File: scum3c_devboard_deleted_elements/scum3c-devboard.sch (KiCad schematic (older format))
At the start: 11 parts, among them P1 Conn_01x03, U9AB1 MPU-9250

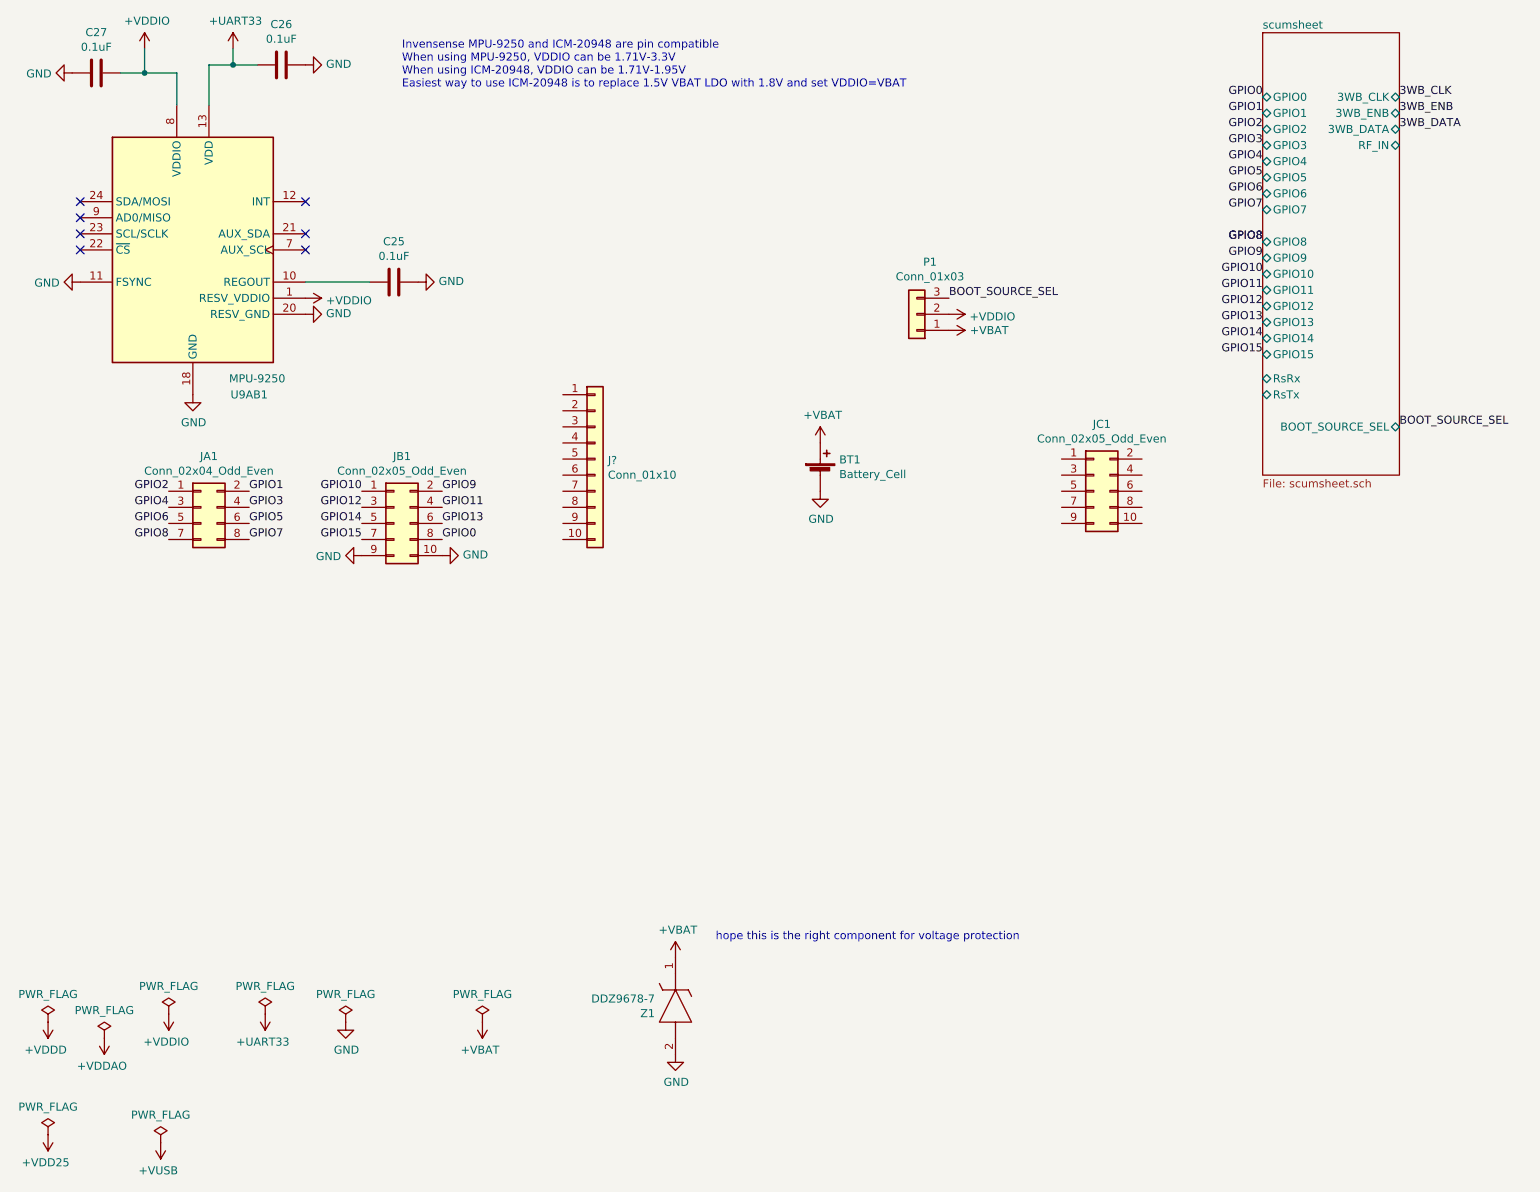
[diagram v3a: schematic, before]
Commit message: moved pins
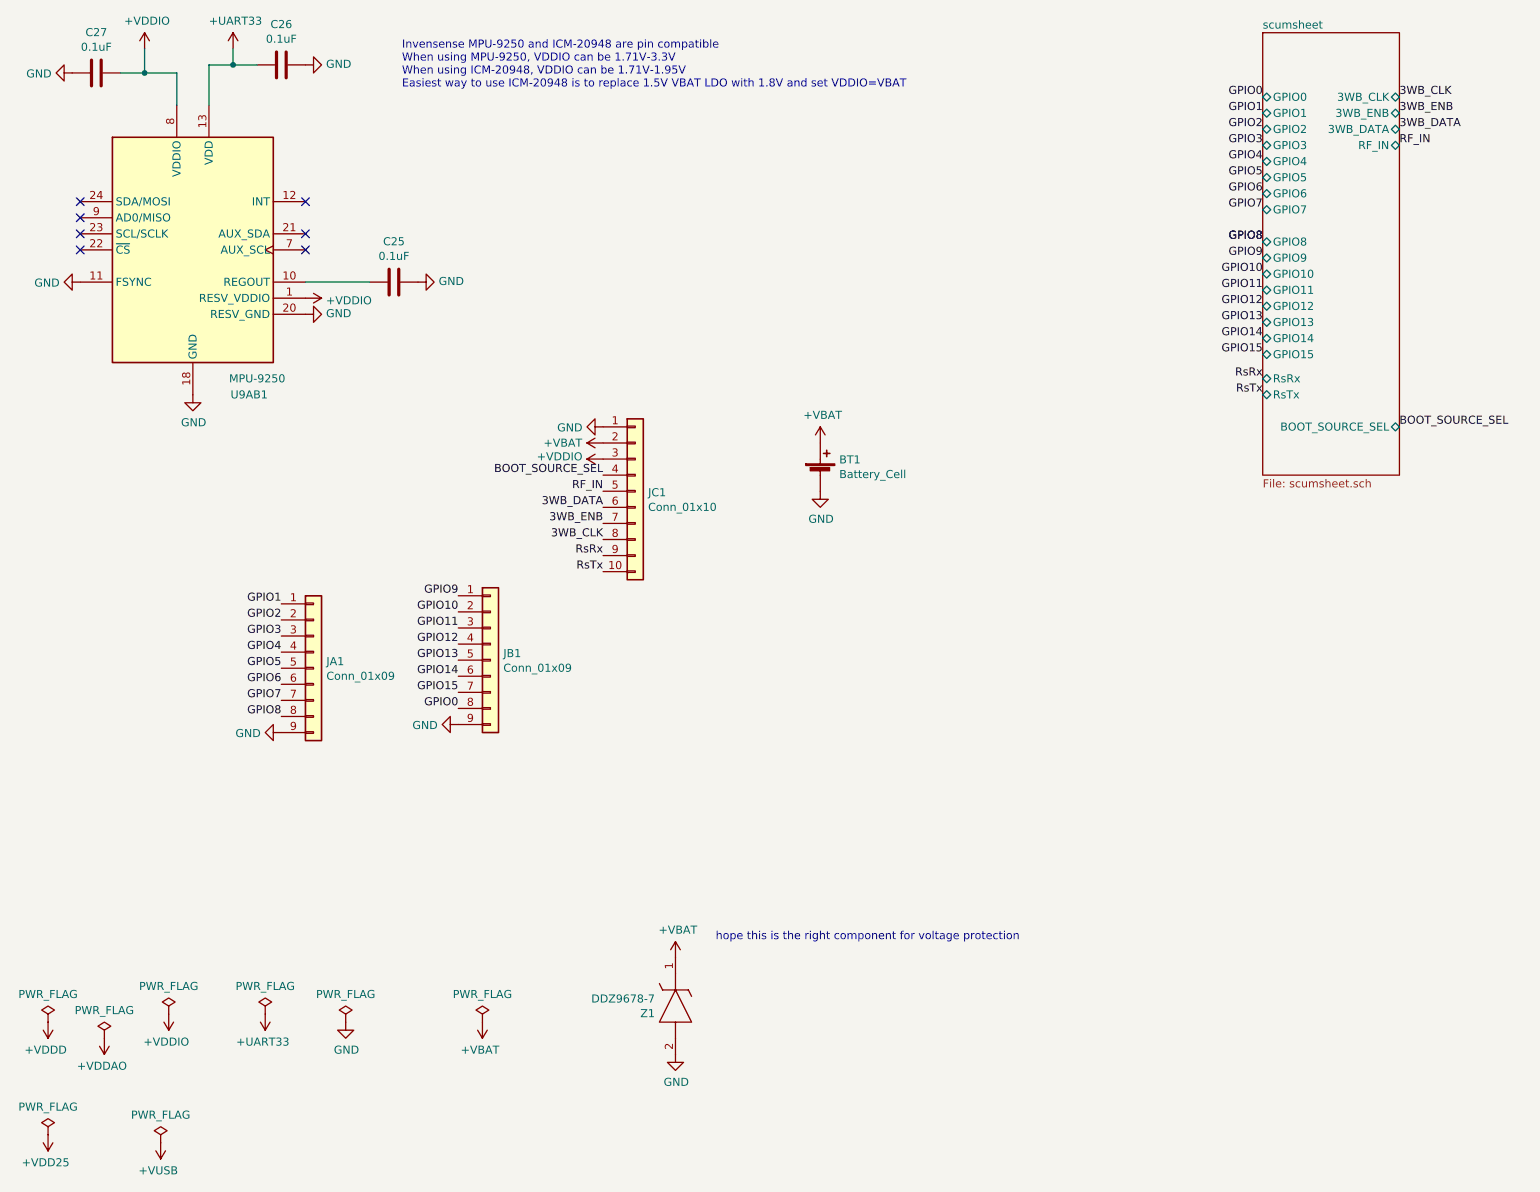
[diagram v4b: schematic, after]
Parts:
- removed JA1: Conn_02x04_Odd_Even, Connector_PinHeader_2.54mm:PinHeader_2x04_P2.54mm_Vertical, symbol Connector_Generic:Conn_02x04_Odd_Even
- removed JB1, JC1: Conn_02x05_Odd_Even, Connector_PinHeader_2.54mm:PinHeader_2x05_P2.54mm_Vertical, symbol Connector_Generic:Conn_02x05_Odd_Even
- removed P1: Conn_01x03, Connector_PinHeader_2.54mm:PinHeader_1x03_P2.54mm_Vertical, symbol Connector_Generic:Conn_01x03
- added JA1, JB1: Conn_01x09, Connector_PinHeader_2.54mm:PinHeader_1x09_P2.54mm_Vertical, symbol Connector_Generic:Conn_01x09
- JC1: renamed from J?; footprint (none) -> Connector_PinHeader_2.54mm:PinHeader_1x10_P2.54mm_Vertical
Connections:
- net +VBAT: now also JC1.2 (Pin_2)
- net +VDDIO: now also JC1.3 (Pin_3)
- net 3WB_CLK: now also JC1.8 (Pin_8)
- net 3WB_DATA: now also JC1.6 (Pin_6)
- net 3WB_ENB: now also JC1.7 (Pin_7)
- net BOOT_SOURCE_SEL: now also JC1.4 (Pin_4)
- net GND: now also JC1.1 (Pin_1), JA1.9 (Pin_9), JB1.9 (Pin_9)
- net GPIO0: now also JB1.8 (Pin_8)
- net GPIO1: now also JA1.1 (Pin_1)
- net GPIO10: now also JB1.2 (Pin_2)
- net GPIO11: now also JB1.3 (Pin_3)
- net GPIO12: now also JB1.4 (Pin_4)
- net GPIO13: now also JB1.5 (Pin_5)
- net GPIO14: now also JB1.6 (Pin_6)
- net GPIO15: now also JB1.7 (Pin_7)
- net GPIO2: now also JA1.2 (Pin_2)
- net GPIO3: now also JA1.3 (Pin_3)
- net GPIO4: now also JA1.4 (Pin_4)
- net GPIO5: now also JA1.5 (Pin_5)
- net GPIO6: now also JA1.6 (Pin_6)
- net GPIO7: now also JA1.7 (Pin_7)
- net GPIO8: now also JA1.8 (Pin_8)
- net GPIO9: now also JB1.1 (Pin_1)
- net RsTx: now reaches JC1.10 (Pin_10)
- net RF_IN: now reaches JC1.5 (Pin_5)
- net RsRx: now reaches JC1.9 (Pin_9)
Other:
- moved on the sheet: JC1
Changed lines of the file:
@@
 	1    0    0    -1
 $EndComp
-Text Label 2950 3650 2    50   ~ 0
+Text Label 3550 4400 2    50   ~ 0
 GPIO10
-Text Label 2950 3750 2    50   ~ 0
+Text Label 3550 4600 2    50   ~ 0
 GPIO12
-Text Label 2950 3850 2    50   ~ 0
+Text Label 3550 4800 2    50   ~ 0
 GPIO14
-Text Label 2950 3950 2    50   ~ 0
+Text Label 3550 4900 2    50   ~ 0
 GPIO15
 $Comp
 L power:GND #PWR0111
 U 1 1 5F3EC8B2
-P 2950 4050
-F 0 "#PWR0111" H 2950 3800 50  0001 C CNN
-F 1 "GND" V 2955 3922 50  0000 R CNN
-F 2 "" H 2950 4050 50  0001 C CNN
-F 3 "" H 2950 4050 50  0001 C CNN
-	1    2950 4050
+P 2450 5150
+F 0 "#PWR0111" H 2450 4900 50  0001 C CNN
+F 1 "GND" V 2455 5022 50  0000 R CNN
+F 2 "" H 2450 5150 50  0001 C CNN
+F 3 "" H 2450 5150 50  0001 C CNN
+	1    2450 5150
 	0    1    1    0
 $EndComp
-Text Label 3450 3650 0    50   ~ 0
+Text Label 3550 4300 2    50   ~ 0
 GPIO9
-Text Label 3450 3950 0    50   ~ 0
+Text Label 3550 5000 2    50   ~ 0
 GPIO0
-Text Label 3450 3850 0    50   ~ 0
+Text Label 3550 4700 2    50   ~ 0
 GPIO13
-Text Label 3450 3750 0    50   ~ 0
+Text Label 3550 4500 2    50   ~ 0
 GPIO11
 $Comp
 L power:GND #PWR0112
 U 1 1 5F3ED1BB
-P 3450 4050
-F 0 "#PWR0112" H 3450 3800 50  0001 C CNN
-F 1 "GND" V 3455 3922 50  0000 R CNN
-F 2 "" H 3450 4050 50  0001 C CNN
-F 3 "" H 3450 4050 50  0001 C CNN
-	1    3450 4050
-	0    -1   -1   0
+P 3550 5100
+F 0 "#PWR0112" H 3550 4850 50  0001 C CNN
+F 1 "GND" V 3555 4972 50  0000 R CNN
+F 2 "" H 3550 5100 50  0001 C CNN
+F 3 "" H 3550 5100 50  0001 C CNN
+	1    3550 5100
+	0    1    1    0
 $EndComp
 $Comp
@@
 	1    0    0    -1
 $EndComp
-$Comp
-L Connector_Generic:Conn_02x04_Odd_Even JA1
-U 1 1 5F4FC0F5
-P 1950 3750
-F 0 "JA1" H 2000 4067 50  0000 C CNN
-F 1 "Conn_02x04_Odd_Even" H 2000 3976 50  0000 C CNN
-F 2 "Connector_PinHeader_2.54mm:PinHeader_2x04_P2.54mm_Vertical" H 1950 3750 50  0001 C CNN
-F 3 "~" H 1950 3750 50  0001 C CNN
-	1    1950 3750
-	1    0    0    -1
-$EndComp
-$Comp
-L Connector_Generic:Conn_02x05_Odd_Even JB1
-U 1 1 5F4FD4BB
-P 3150 3850
-F 0 "JB1" H 3200 4267 50  0000 C CNN
-F 1 "Conn_02x05_Odd_Even" H 3200 4176 50  0000 C CNN
-F 2 "Connector_PinHeader_2.54mm:PinHeader_2x05_P2.54mm_Vertical" H 3150 3850 50  0001 C CNN
-F 3 "~" H 3150 3850 50  0001 C CNN
-	1    3150 3850
-	1    0    0    -1
-$EndComp
 Text Label 8550 2600 2    50   ~ 0
 GPIO13
@@
 L draft1library:+VBAT #PWR?
 U 1 1 5F7B958D
-P 6600 2650
+P 4450 3350
 AR Path="/5F3B1D81/5F7B958D" Ref="#PWR?"  Part="1"
 AR Path="/5F41418C/5F7B958D" Ref="#PWR?"  Part="1"
 AR Path="/5F414989/5F7B958D" Ref="#PWR?"  Part="1"
 AR Path="/5F7B958D" Ref="#PWR0109"  Part="1"
-F 0 "#PWR0109" H 6600 2500 50  0001 C CNN
-F 1 "+VBAT" V 6600 2900 50  0000 C CNN
-F 2 "" H 6600 2650 50  0001 C CNN
-F 3 "" H 6600 2650 50  0001 C CNN
-	1    6600 2650
-	0    1    1    0
-$EndComp
-Text Label 6600 2450 0    50   ~ 0
+F 0 "#PWR0109" H 4450 3200 50  0001 C CNN
+F 1 "+VBAT" V 4450 3600 50  0000 C CNN
+F 2 "" H 4450 3350 50  0001 C CNN
+F 3 "" H 4450 3350 50  0001 C CNN
+	1    4450 3350
+	0    -1   -1   0
+$EndComp
+Text Label 4450 3550 2    50   ~ 0
 BOOT_SOURCE_SEL
-$Comp
-L Connector_Generic:Conn_01x03 P?
-U 1 1 5F7B9594
-P 6400 2550
-AR Path="/5F3B1D81/5F7B9594" Ref="P?"  Part="1"
-AR Path="/5F7B9594" Ref="P1"  Part="1"
-F 0 "P1" H 6318 2225 50  0000 C CNN
-F 1 "Conn_01x03" H 6318 2316 50  0000 C CNN
-F 2 "Connector_PinHeader_2.54mm:PinHeader_1x03_P2.54mm_Vertical" H 6400 2550 50  0001 C CNN
-F 3 "~" H 6400 2550 50  0001 C CNN
-	1    6400 2550
-	-1   0    0    1
-$EndComp
 $Comp
 L draft1library:+VDDIO #PWR?
 U 1 1 5F7B959A
-P 6600 2550
+P 4450 3450
 AR Path="/5F3B1D81/5F7B959A" Ref="#PWR?"  Part="1"
 AR Path="/5F7B959A" Ref="#PWR0110"  Part="1"
-F 0 "#PWR0110" H 6600 2400 50  0001 C CNN
-F 1 "+VDDIO" V 6615 2678 50  0000 L CNN
-F 2 "" H 6600 2550 50  0001 C CNN
-F 3 "" H 6600 2550 50  0001 C CNN
-	1    6600 2550
-	0    1    1    0
+F 0 "#PWR0110" H 4450 3300 50  0001 C CNN
+F 1 "+VDDIO" V 4465 3578 50  0000 L CNN
+F 2 "" H 4450 3450 50  0001 C CNN
+F 3 "" H 4450 3450 50  0001 C CNN
+	1    4450 3450
+	0    -1   -1   0
 $EndComp
 Text Label 9400 3250 0    50   ~ 0
 BOOT_SOURCE_SEL
 $Comp
-L Connector_Generic:Conn_02x05_Odd_Even JC1
-U 1 1 5F7BA02A
-P 7500 3650
-F 0 "JC1" H 7550 4067 50  0000 C CNN
-F 1 "Conn_02x05_Odd_Even" H 7550 3976 50  0000 C CNN
-F 2 "Connector_PinHeader_2.54mm:PinHeader_2x05_P2.54mm_Vertical" H 7500 3650 50  0001 C CNN
-F 3 "~" H 7500 3650 50  0001 C CNN
-	1    7500 3650
-	1    0    0    -1
-$EndComp
-$Comp
-L Connector_Generic:Conn_01x10 J?
+L Connector_Generic:Conn_01x10 JC1
 U 1 1 5F7BC634
-P 4400 3450
-F 0 "J?" H 4480 3442 50  0000 L CNN
-F 1 "Conn_01x10" H 4480 3351 50  0000 L CNN
-F 2 "" H 4400 3450 50  0001 C CNN
-F 3 "~" H 4400 3450 50  0001 C CNN
-	1    4400 3450
-	1    0    0    -1
-$EndComp
-Text Label 2250 3750 0    50   ~ 0
+P 4650 3650
+F 0 "JC1" H 4730 3642 50  0000 L CNN
+F 1 "Conn_01x10" H 4730 3551 50  0000 L CNN
+F 2 "Connector_PinHeader_2.54mm:PinHeader_1x10_P2.54mm_Vertical" H 4650 3650 50  0001 C CNN
+F 3 "~" H 4650 3650 50  0001 C CNN
+	1    4650 3650
+	1    0    0    -1
+$EndComp
+Text Label 2450 4550 2    50   ~ 0
 GPIO3
-Text Label 2250 3850 0    50   ~ 0
+Text Label 2450 4750 2    50   ~ 0
 GPIO5
-Text Label 2250 3950 0    50   ~ 0
+Text Label 2450 4950 2    50   ~ 0
 GPIO7
-Text Label 2250 3650 0    50   ~ 0
+Text Label 2450 4350 2    50   ~ 0
 GPIO1
-Text Label 1750 3950 2    50   ~ 0
+Text Label 2450 4450 2    50   ~ 0
+GPIO2
+Text Label 2450 4650 2    50   ~ 0
+GPIO4
+Text Label 2450 4850 2    50   ~ 0
+GPIO6
+Text Label 2450 5050 2    50   ~ 0
 GPIO8
-Text Label 1750 3850 2    50   ~ 0
-GPIO6
-Text Label 1750 3750 2    50   ~ 0
-GPIO4
-Text Label 1750 3650 2    50   ~ 0
-GPIO2
+Text Label 9400 1500 0    50   ~ 0
+RF_IN
+Text Label 8550 2950 2    50   ~ 0
+RsRx
+Text Label 8550 3050 2    50   ~ 0
+RsTx
+$Comp
+L Connector_Generic:Conn_01x09 JA1
+U 1 1 5F7CC956
+P 2650 4750
+F 0 "JA1" H 2730 4792 50  0000 L CNN
+F 1 "Conn_01x09" H 2730 4701 50  0000 L CNN
+F 2 "Connector_PinHeader_2.54mm:PinHeader_1x09_P2.54mm_Vertical" H 2650 4750 50  0001 C CNN
+F 3 "~" H 2650 4750 50  0001 C CNN
+	1    2650 4750
+	1    0    0    -1
+$EndComp
+$Comp
+L Connector_Generic:Conn_01x09 JB1
+U 1 1 5F7CF946
+P 3750 4700
+F 0 "JB1" H 3830 4742 50  0000 L CNN
+F 1 "Conn_01x09" H 3830 4651 50  0000 L CNN
+F 2 "Connector_PinHeader_2.54mm:PinHeader_1x09_P2.54mm_Vertical" H 3750 4700 50  0001 C CNN
+F 3 "~" H 3750 4700 50  0001 C CNN
+	1    3750 4700
+	1    0    0    -1
+$EndComp
+$Comp
+L power:GND #PWR0124
+U 1 1 5F7D3632
+P 4450 3250
+F 0 "#PWR0124" H 4450 3000 50  0001 C CNN
+F 1 "GND" V 4455 3122 50  0000 R CNN
+F 2 "" H 4450 3250 50  0001 C CNN
+F 3 "" H 4450 3250 50  0001 C CNN
+	1    4450 3250
+	0    1    1    0
+$EndComp
+Text Label 4450 4050 2    50   ~ 0
+RsRx
+Text Label 4450 4150 2    50   ~ 0
+RsTx
+Text Label 4450 3950 2    50   ~ 0
+3WB_CLK
+Text Label 4450 3850 2    50   ~ 0
+3WB_ENB
+Text Label 4450 3750 2    50   ~ 0
+3WB_DATA
+Text Label 4450 3650 2    50   ~ 0
+RF_IN
 $EndSCHEMATC
